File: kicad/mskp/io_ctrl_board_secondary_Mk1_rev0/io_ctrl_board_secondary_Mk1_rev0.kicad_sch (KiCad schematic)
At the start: 9 parts, among them J1 OLED_128x64, J2 USB_C_Receptacle_USB2.0, J3 Conn_01x12_Socket, SW1 SW_Omron_B3FS, U1 MCP23017_SP

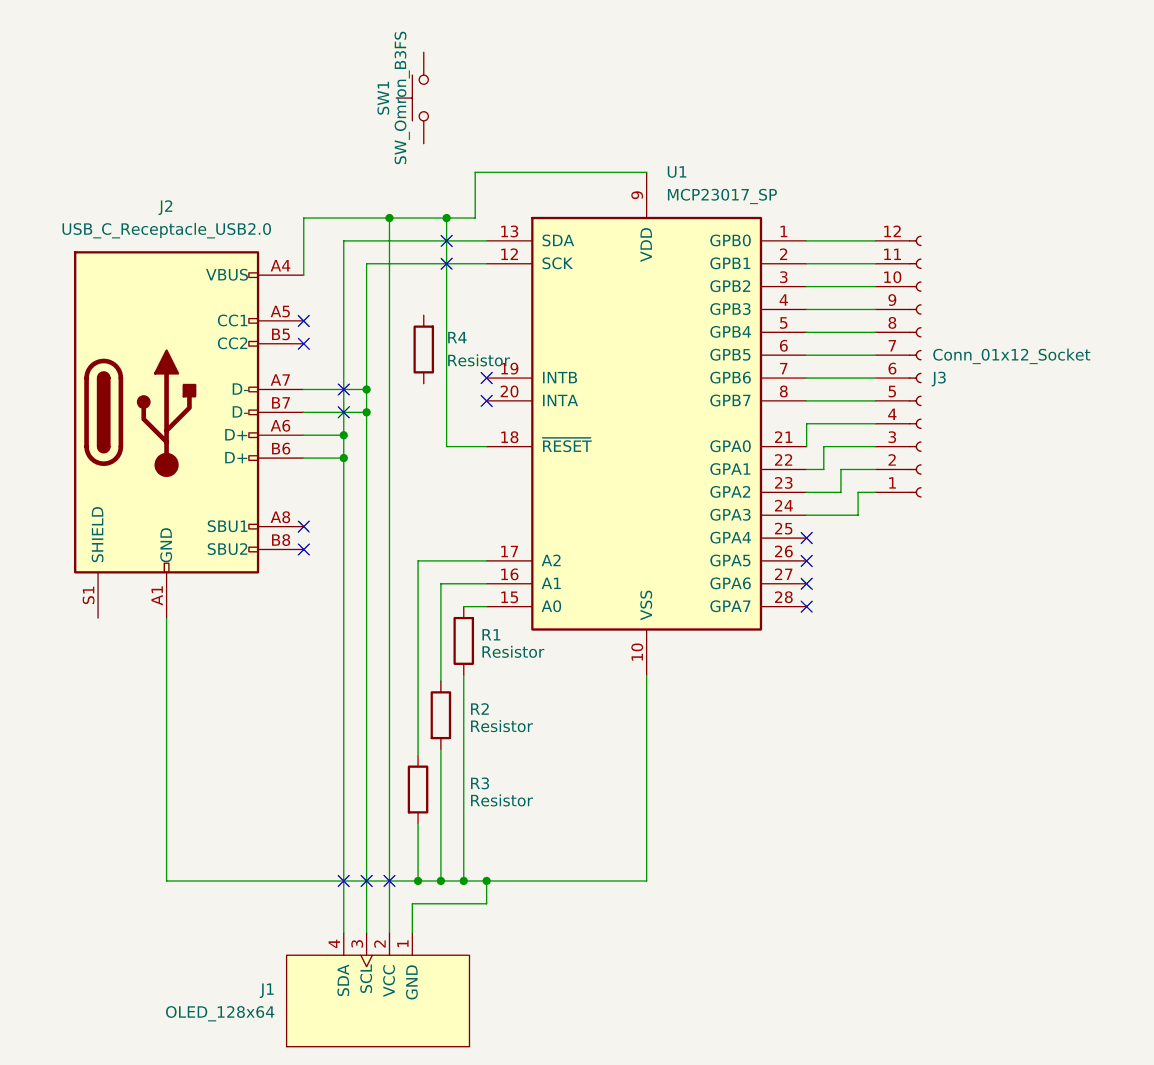
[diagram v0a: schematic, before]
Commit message: Adds work on io_ctrl_board_secondary_Mk1_rev0 pcb
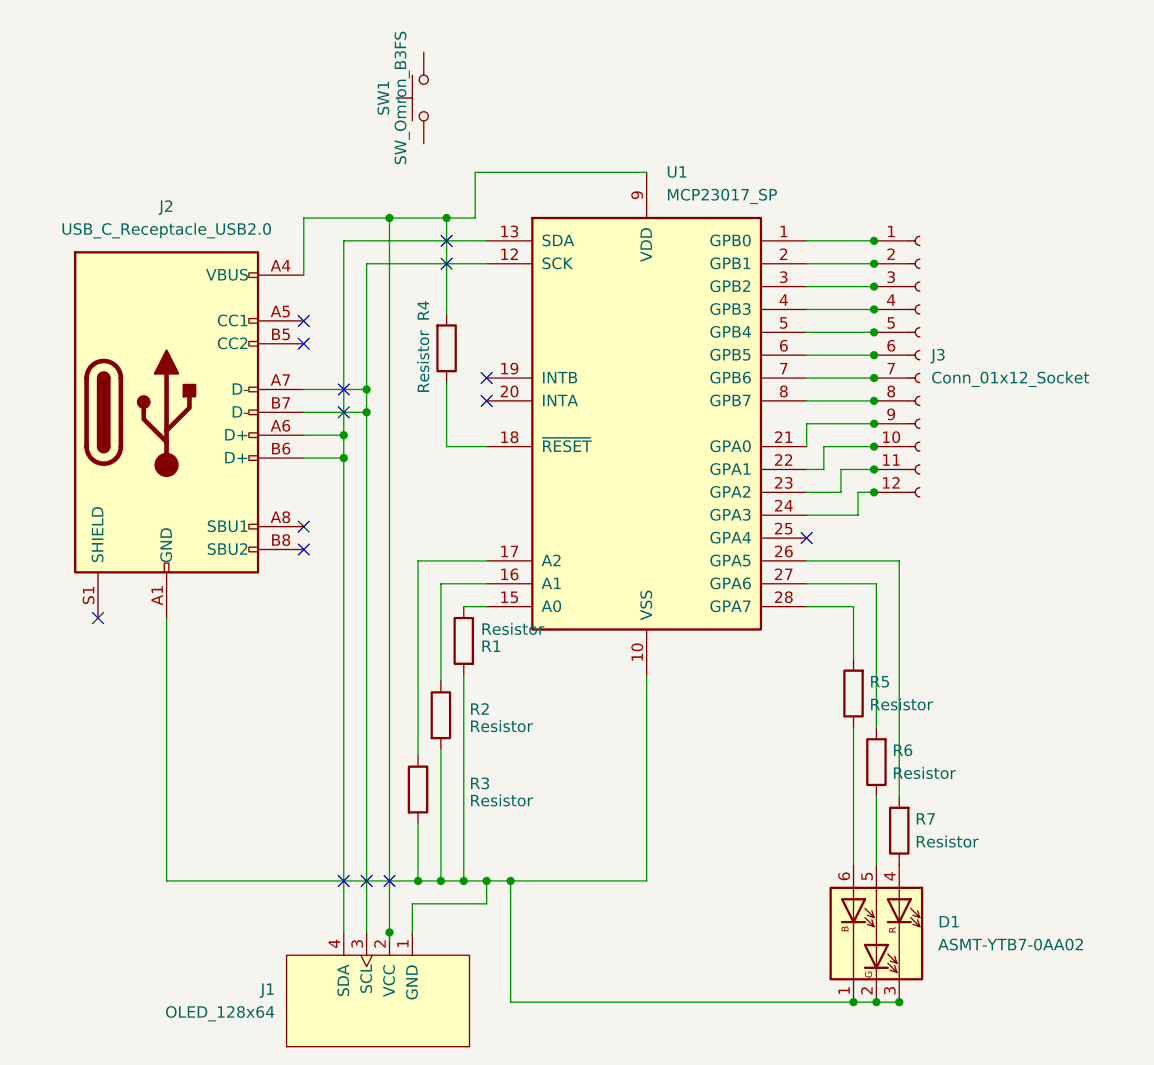
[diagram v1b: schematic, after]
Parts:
- added D1: ASMT-YTB7-0AA02, LED_SMD:LED_Avago_PLCC6_3x2.8mm, symbol LED:ASMT-YTB7-0AA02
- added R5, R6, R7: Resistor, Resistor_THT:R_Axial_DIN0204_L3.6mm_D1.6mm_P5.08mm_Horizontal, symbol ScottoKeebs:Placeholder_Resistor
- J2: footprint (none) -> Connector_USB:USB_C_Receptacle_GCT_USB4110
- J3: footprint (none) -> Connector_JST:JST_GH_SM12B-GHS-TB_1x12-1MP_P1.25mm_Horizontal
- R1, R2, R3, R4: footprint (none) -> Resistor_THT:R_Axial_DIN0204_L3.6mm_D1.6mm_P5.08mm_Horizontal
- SW1: footprint (none) -> Button_Switch_SMD:SW_SPST_Omron_B3FS-101xP
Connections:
- net at J1.1 (GND), J2.A1 (GND), J2.A12 (GND)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: now also R1.2, D1.1 (KB), D1.2 (KG), D1.3 (KR); no longer R1.1
- net at J1.2 (VCC), J2.A4 (VBUS), J2.A9 (VBUS)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: now also R4.2; no longer U1.18 (~{RESET})
- net at R4.1: now also U1.18 (~{RESET})
- net at J3.1 (Pin_1): now also U1.1 (GPB0); no longer U1.24 (GPA3)
- net at J3.10 (Pin_10): now also U1.22 (GPA1); no longer U1.3 (GPB2)
- net at J3.11 (Pin_11): now also U1.23 (GPA2); no longer U1.2 (GPB1)
- net at J3.12 (Pin_12): now also U1.24 (GPA3); no longer U1.1 (GPB0)
- net at J3.2 (Pin_2): now also U1.2 (GPB1); no longer U1.23 (GPA2)
- net at J3.3 (Pin_3): now also U1.3 (GPB2); no longer U1.22 (GPA1)
- net at J3.4 (Pin_4): now also U1.4 (GPB3); no longer U1.21 (GPA0)
- net at J3.5 (Pin_5): now also U1.5 (GPB4); no longer U1.8 (GPB7)
- net at J3.6 (Pin_6): now also U1.6 (GPB5); no longer U1.7 (GPB6)
- net at J3.7 (Pin_7): now also U1.7 (GPB6); no longer U1.6 (GPB5)
- net at J3.8 (Pin_8): now also U1.8 (GPB7); no longer U1.5 (GPB4)
- net at J3.9 (Pin_9): now also U1.21 (GPA0); no longer U1.4 (GPB3)
- net at U1.15 (A0): now also R1.1; no longer R1.2
- net at U1.26 (GPA5): now also R7.2
- net at U1.27 (GPA6): now also R6.2
- net at U1.28 (GPA7): now also R5.2
- new net: D1.4 (AR), R7.1
- new net: D1.6 (AB), R5.1
- new net: D1.5 (AG), R6.1
- no-connect marks 17 -> 15
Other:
- moved on the sheet: R4

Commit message: More work on io_ctrl_board_secondary_Mk1_rev0 layout and schema
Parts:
- added Q1: 2N3904, Package_TO_SOT_THT:TO-92_Inline, symbol Transistor_BJT:2N3904
- added R8: 100K, Resistor_THT:R_Axial_DIN0204_L3.6mm_D1.6mm_P5.08mm_Horizontal, symbol ScottoKeebs:Placeholder_Resistor
- R1, R2, R3, R4: value Resistor -> 10k
- R5, R6, R7: value Resistor -> ?k
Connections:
- net at D1.1 (KB), D1.2 (KG), D1.3 (KR)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: now also SW1.2
- net at J2.A4 (VBUS), J2.A9 (VBUS), J2.B4 (VBUS)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: now also Q1.3 (C), R8.2; no longer J1.2 (VCC), R4.2, U1.9 (VDD)
- net at R4.1: now also J1.2 (VCC), U1.9 (VDD), Q1.1 (E); no longer U1.18 (~{RESET})
- net at SW1.1: now also Q1.2 (B), R8.1
- new net: R4.2, U1.18 (~{RESET})
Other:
- moved on the sheet: R4, SW1

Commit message: Adds logo and OSH symbol to all mskp silkscreens
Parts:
- U1: footprint Package_DIP:DIP-28_W7.62mm -> Package_DIP:DIP-28_W7.62mm_Socket
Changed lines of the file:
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@@
       (effects (font (size 1.27 1.27)) (justify left))
     )
-    (property "Footprint" "Package_DIP:DIP-28_W7.62mm" (at 153.035 100.33 0)
+    (property "Footprint" "Package_DIP:DIP-28_W7.62mm_Socket" (at 153.035 100.33 0)
       (effects (font (size 1.27 1.27)) (justify left) hide)
     )

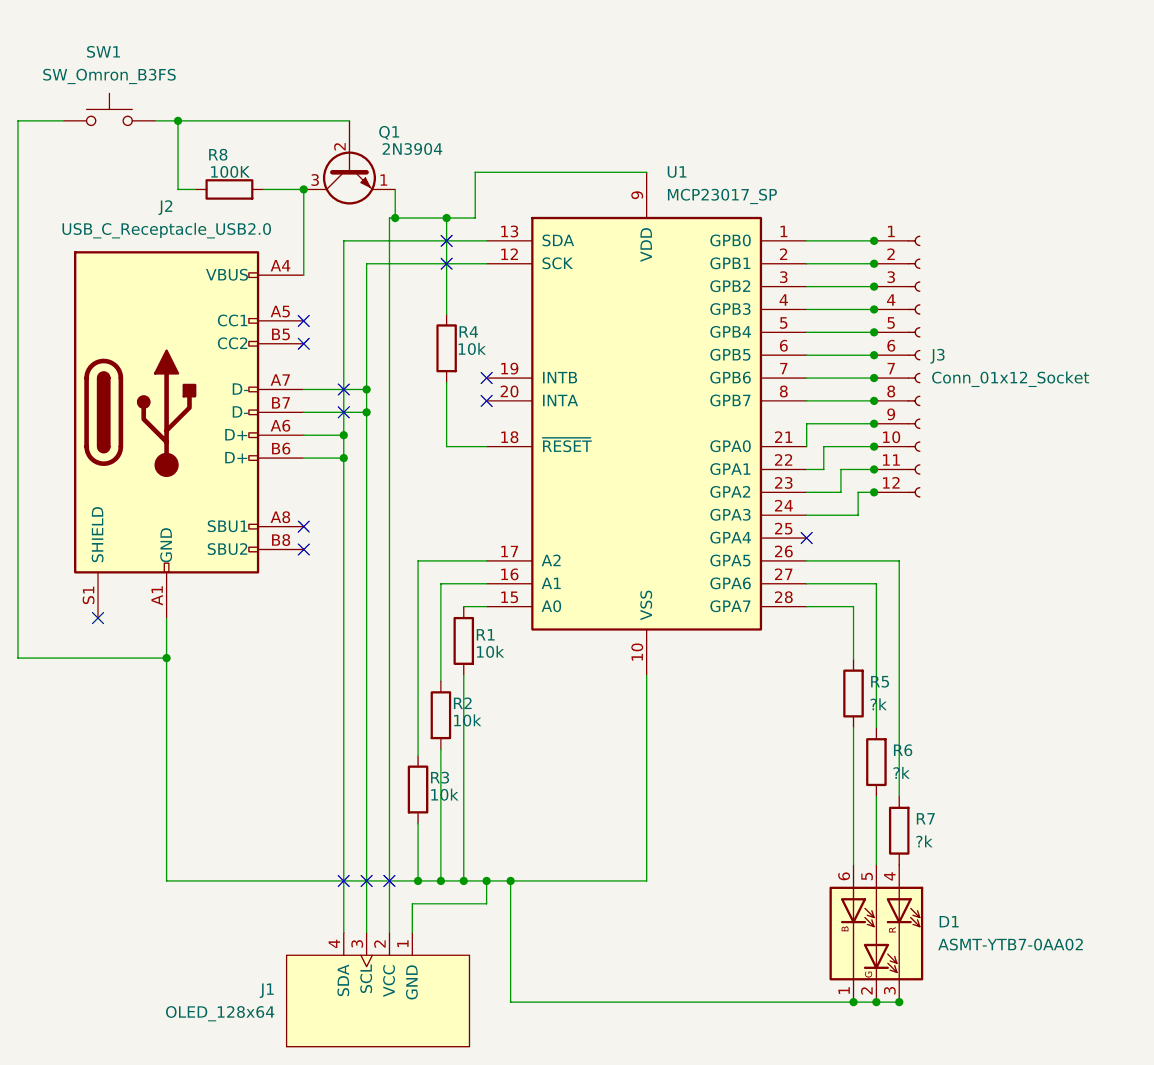
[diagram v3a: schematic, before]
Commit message: Adds wiring for io_ctrl_board_secondary_Mk1_rev0
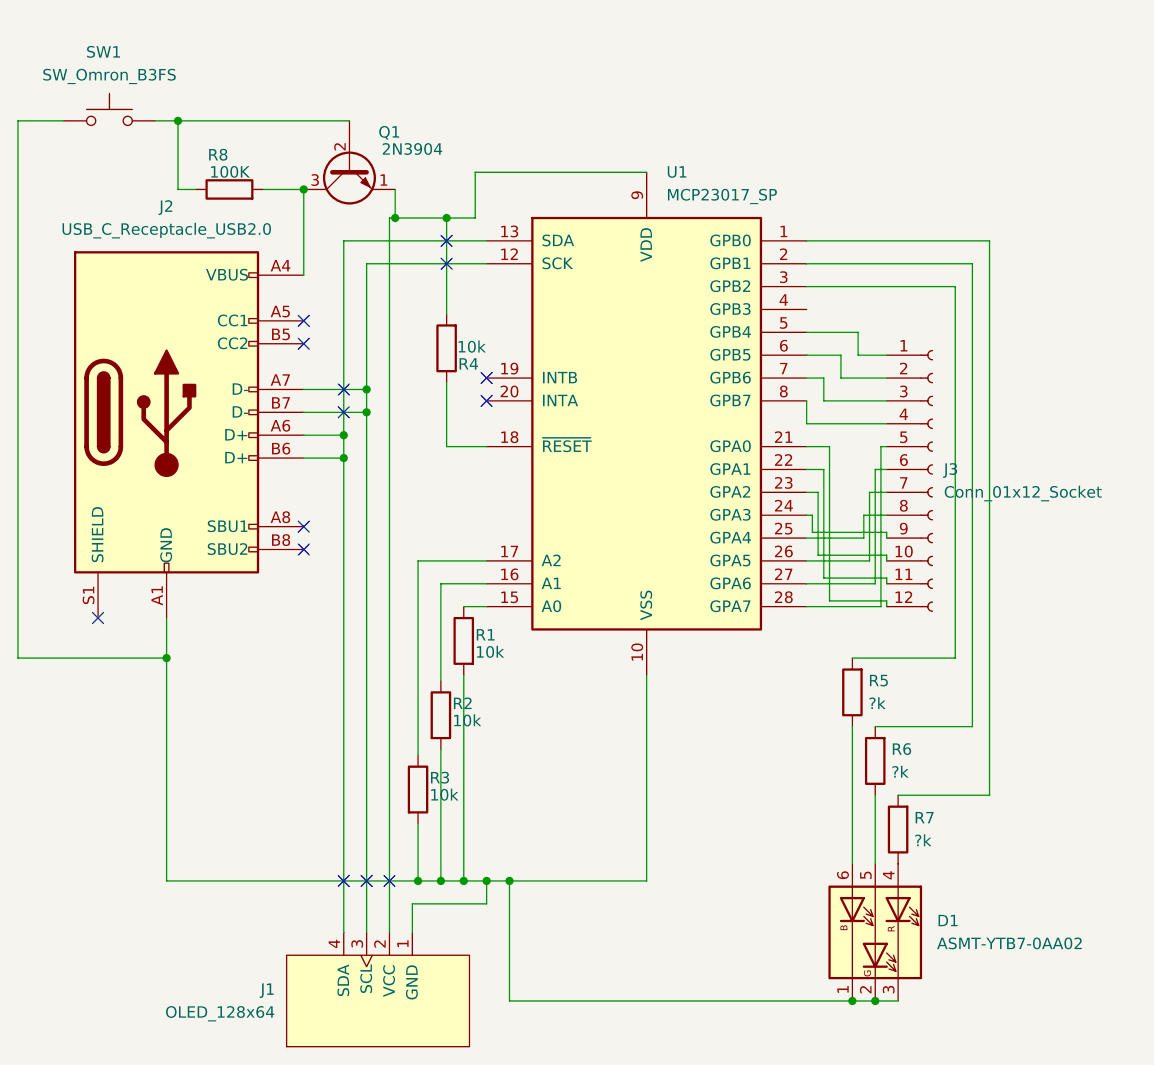
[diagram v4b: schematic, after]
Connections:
- net at R7.2: now also U1.1 (GPB0); no longer U1.26 (GPA5)
- net at R5.2: now also U1.3 (GPB2); no longer U1.28 (GPA7)
- net at J1.2 (VCC), Q1.1 (E), U1.9 (VDD): now also R4.2; no longer R4.1
- net at R6.2: now also U1.2 (GPB1); no longer U1.27 (GPA6)
- net at U1.18 (~{RESET}): now also R4.1; no longer R4.2
- net at J3.1 (Pin_1): now also U1.5 (GPB4); no longer U1.1 (GPB0)
- net at J3.10 (Pin_10): now also U1.23 (GPA2); no longer U1.22 (GPA1)
- net at J3.11 (Pin_11): now also U1.22 (GPA1); no longer U1.23 (GPA2)
- net at J3.12 (Pin_12): now also U1.21 (GPA0); no longer U1.24 (GPA3)
- net at J3.2 (Pin_2): now also U1.6 (GPB5); no longer U1.2 (GPB1)
- net at J3.3 (Pin_3): now also U1.7 (GPB6); no longer U1.3 (GPB2)
- net at J3.4 (Pin_4): now also U1.8 (GPB7); no longer U1.4 (GPB3)
- net at J3.5 (Pin_5): now also U1.28 (GPA7); no longer U1.5 (GPB4)
- net at J3.6 (Pin_6): now also U1.27 (GPA6); no longer U1.6 (GPB5)
- net at J3.7 (Pin_7): now also U1.26 (GPA5); no longer U1.7 (GPB6)
- net at J3.8 (Pin_8): now also U1.25 (GPA4); no longer U1.8 (GPB7)
- net at J3.9 (Pin_9): now also U1.24 (GPA3); no longer U1.21 (GPA0)
- no-connect marks 15 -> 14
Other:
- moved on the sheet: J3
